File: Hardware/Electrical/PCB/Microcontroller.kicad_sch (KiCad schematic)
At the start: 4 parts, among them U4 ESP32-S3-WROOM-1, U5 CAP1296-1-AIA-TR

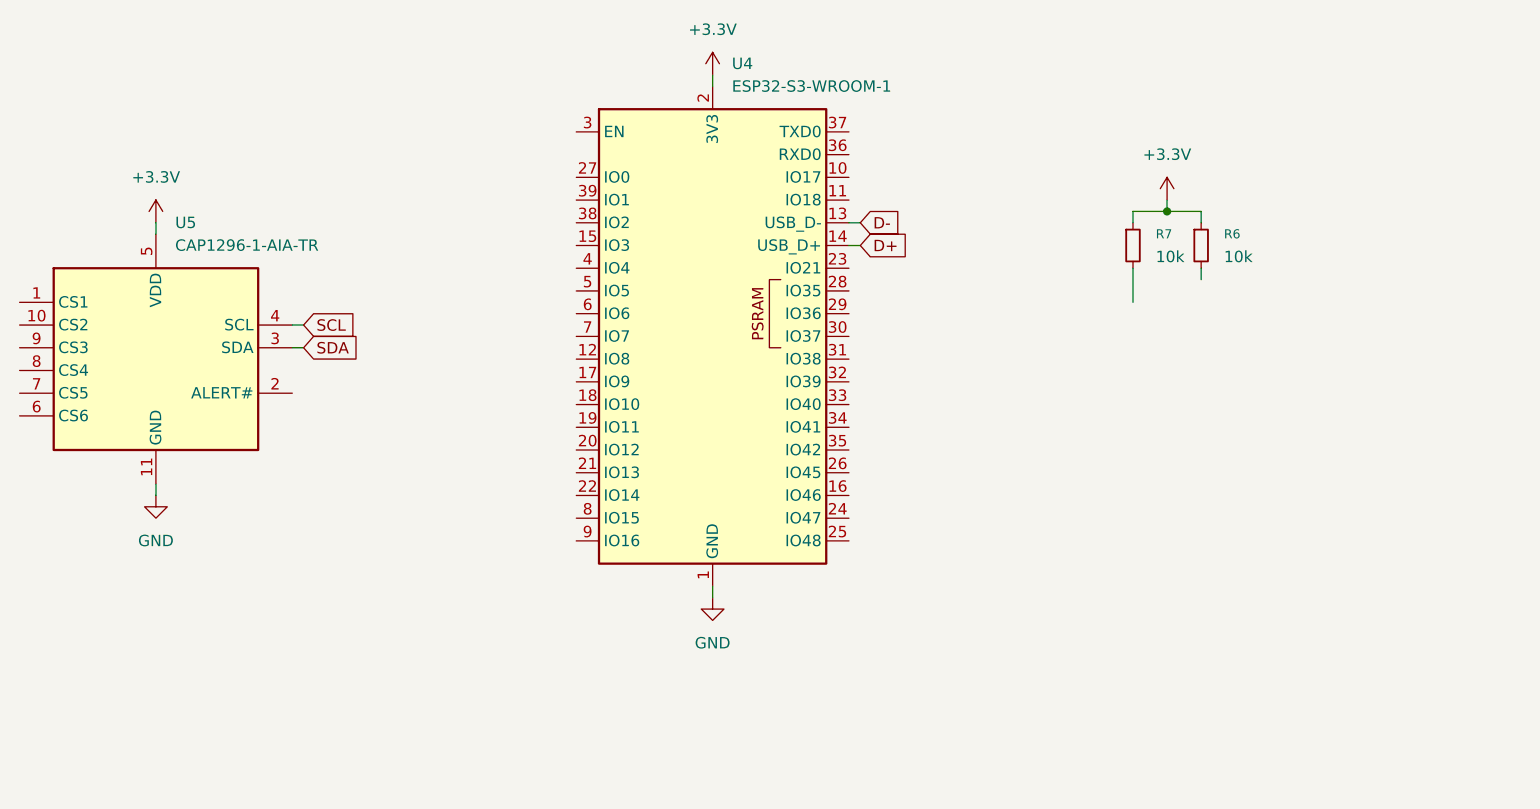
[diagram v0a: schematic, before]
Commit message: Basic Schematic finished, external connectors missing, no footprints or LCSC numbers yet
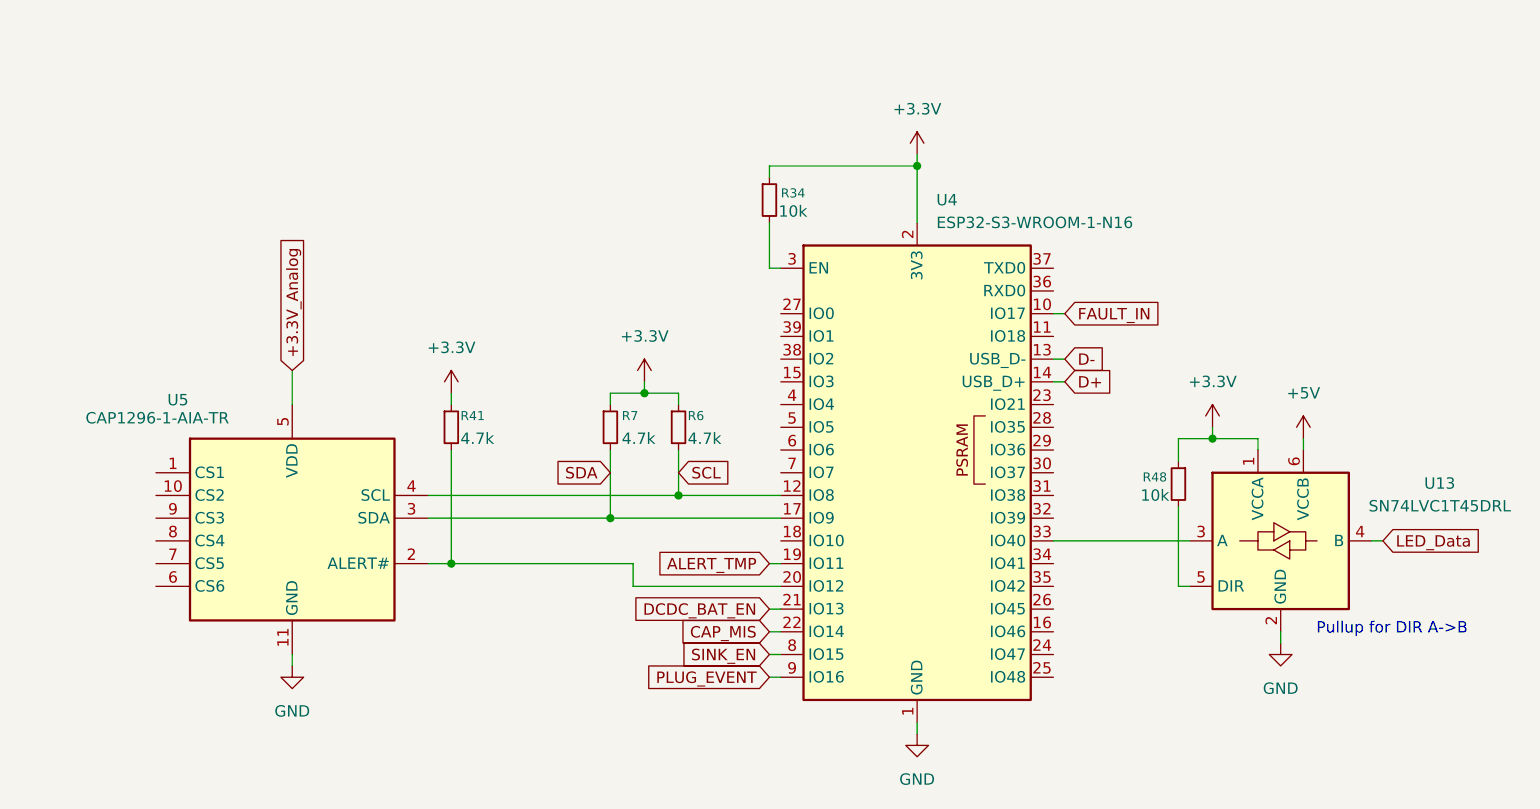
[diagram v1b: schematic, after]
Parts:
- added R34, R48: 10k, symbol Device:R_Small
- added R41: 4.7k, symbol Device:R_Small
- added U13: SN74LVC1T45DRL, Package_TO_SOT_SMD:SOT-563, symbol Logic_LevelTranslator:SN74LVC1T45DRL
- R6, R7: value 10k -> 4.7k
- U4: value ESP32-S3-WROOM-1 -> ESP32-S3-WROOM-1-N16
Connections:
- net +3.3V: now also R34.1, R41.1, R48.1, U13.1 (VCCA); no longer U5.5 (VDD)
- net GND: now also U13.2 (GND)
- net SCL: now also R6.2, U4.12 (IO8)
- net SDA: now also R7.2, U4.17 (IO9)
- net FAULT_IN: now reaches U4.10 (IO17)
- net ALERT_TMP: now reaches U4.19 (IO11)
- net at U4.20 (IO12): now also U5.2 (ALERT#), R41.2
- net DCDC_BAT_EN: now reaches U4.21 (IO13)
- net CAP_MIS: now reaches U4.22 (IO14)
- net at U4.3 (EN): now also R34.2
- net at U4.33 (IO40): now also U13.3 (A)
- net SINK_EN: now reaches U4.8 (IO15)
- net PLUG_EVENT: now reaches U4.9 (IO16)
- new net: R48.2, U13.5 (DIR)
- new net +3.3V_Analog: U5.5 (VDD)
- new net +5V: U13.6 (VCCB)
- new net LED_Data: U13.4 (B)
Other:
- note added: "Pullup for DIR A->B"
- moved on the sheet: R6, R7, U4, U5

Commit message: layout v1 finished but not confirmed yet
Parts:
- added J2, J3, J4, J5, J6, J7: 1, Connector_JST:JST_XH_B1B-XH-AM_1x01_P2.50mm_Vertical, symbol Connector_Generic:Conn_01x01
- R34, R48: footprint (none) -> Resistor_SMD:R_0603_1608Metric; *LCSC Part Number (none) -> C25804
- R41, R6, R7: footprint (none) -> Resistor_SMD:R_0603_1608Metric; *LCSC Part Number (none) -> C23162
- U13: *LCSC Part Number (none) -> C352970
- U4: *LCSC Part Number (none) -> C2913199
- U5: *LCSC Part Number (none) -> C2652051
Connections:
- net EN_BAT: now reaches U4.16 (IO46)
- net PG_USBC: now reaches U4.24 (IO47)
- net PG_BAT: now reaches U4.25 (IO48)
- net CT_1: now reaches U5.1 (CS1)
- net CT_1: now also J2.1 (Pin_1)
- net CT_2: now reaches U5.10 (CS2)
- net CT_2: now also J3.1 (Pin_1)
- net CT_6: now reaches U5.6 (CS6)
- net CT_6: now also J7.1 (Pin_1)
- net CT_5: now reaches U5.7 (CS5)
- net CT_5: now also J6.1 (Pin_1)
- net CT_4: now reaches U5.8 (CS4)
- net CT_4: now also J5.1 (Pin_1)
- net CT_3: now reaches U5.9 (CS3)
- net CT_3: now also J4.1 (Pin_1)
- no-connect marks 0 -> 21
